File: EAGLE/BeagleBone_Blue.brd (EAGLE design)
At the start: 86.4 x 54.6 mm, 302 parts, among them J2 SERVO_HEADERS_8X, M1 JST_ZH_2, M2 JST_ZH_2, M3 JST_ZH_2, M4 JST_ZH_2, Q1 MOSFET-N, U1 TCAN1051HV, U10 TXS0108ERGYR, U13 EMMC, U2 SN74LV1T126DBVR, U3 TPD4S012DRY, U4 TPD4S012DRY, U5 24LC_32AT-I/OT, U6 SN74LVC1G07_DCK_5, U7 WL1835MODGBMOCT, U8 TPS2105_DBV_5, U9 TXS0108ERGYR, X2 SCHA5B0200, X3 USB1, X4 10118192-0001LF, Y1 24 MHz, Y2 32.768kHz

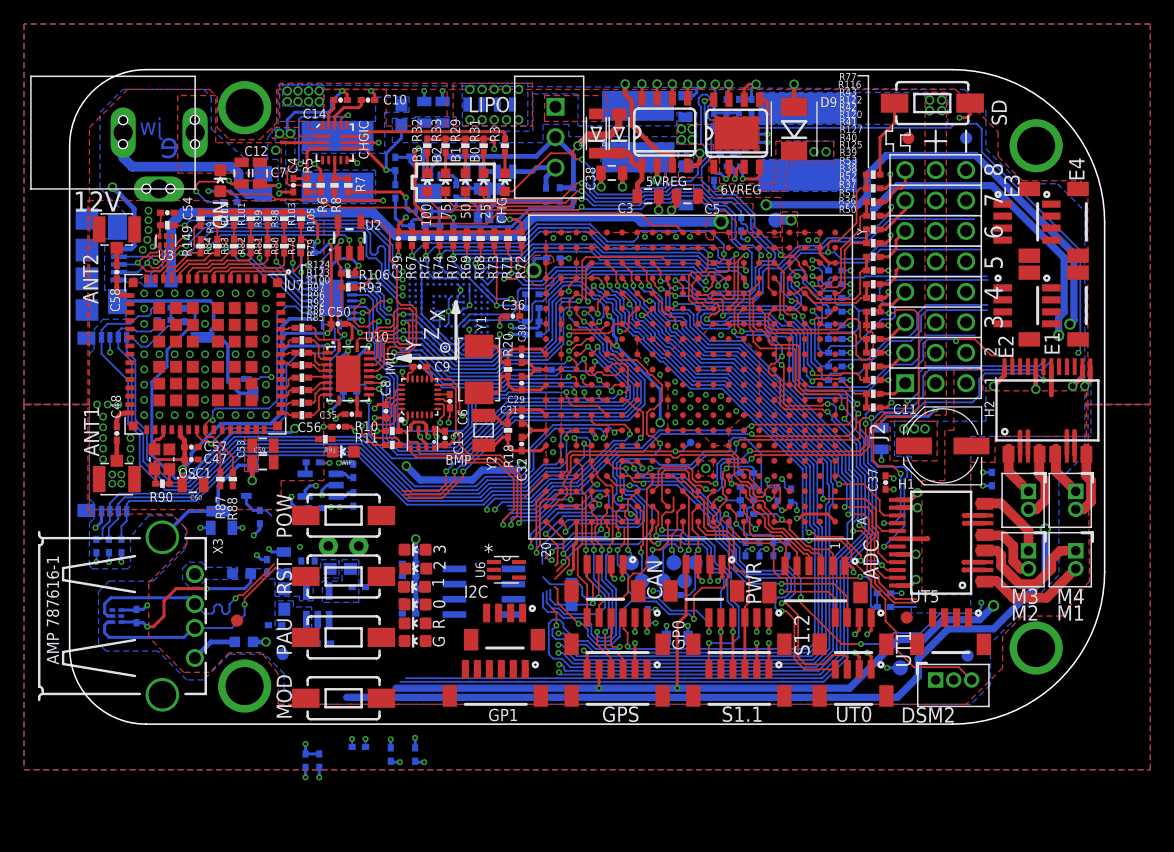
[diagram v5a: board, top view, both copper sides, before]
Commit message: Cleaned up top side silkscreen
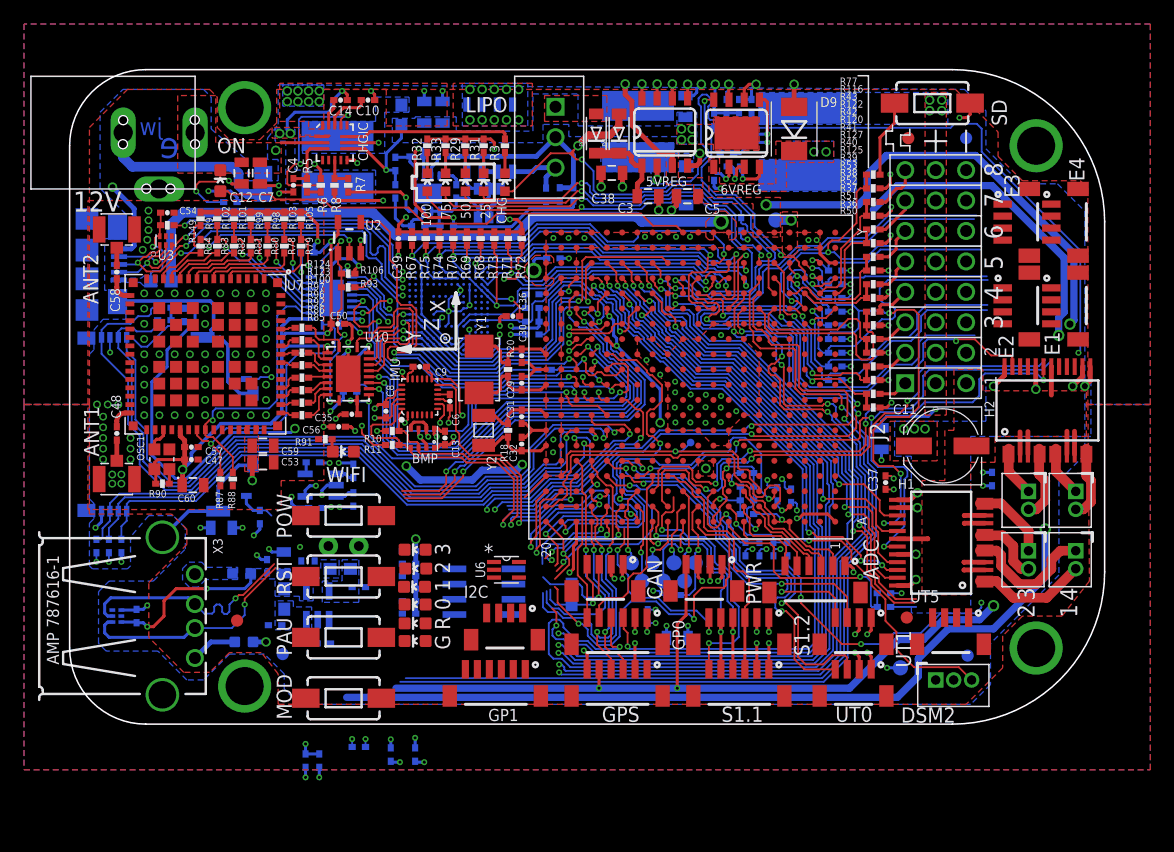
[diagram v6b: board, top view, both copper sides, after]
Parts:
- moved U$5 0.76 mm to (32.2, -23.3)
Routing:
- net N$20: track 0.00 -> 1.10 mm
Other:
- board text added: "1"
- board text added: "2"
- board text added: "3"
- board text added: "4"

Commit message: Updates to silkscreen.
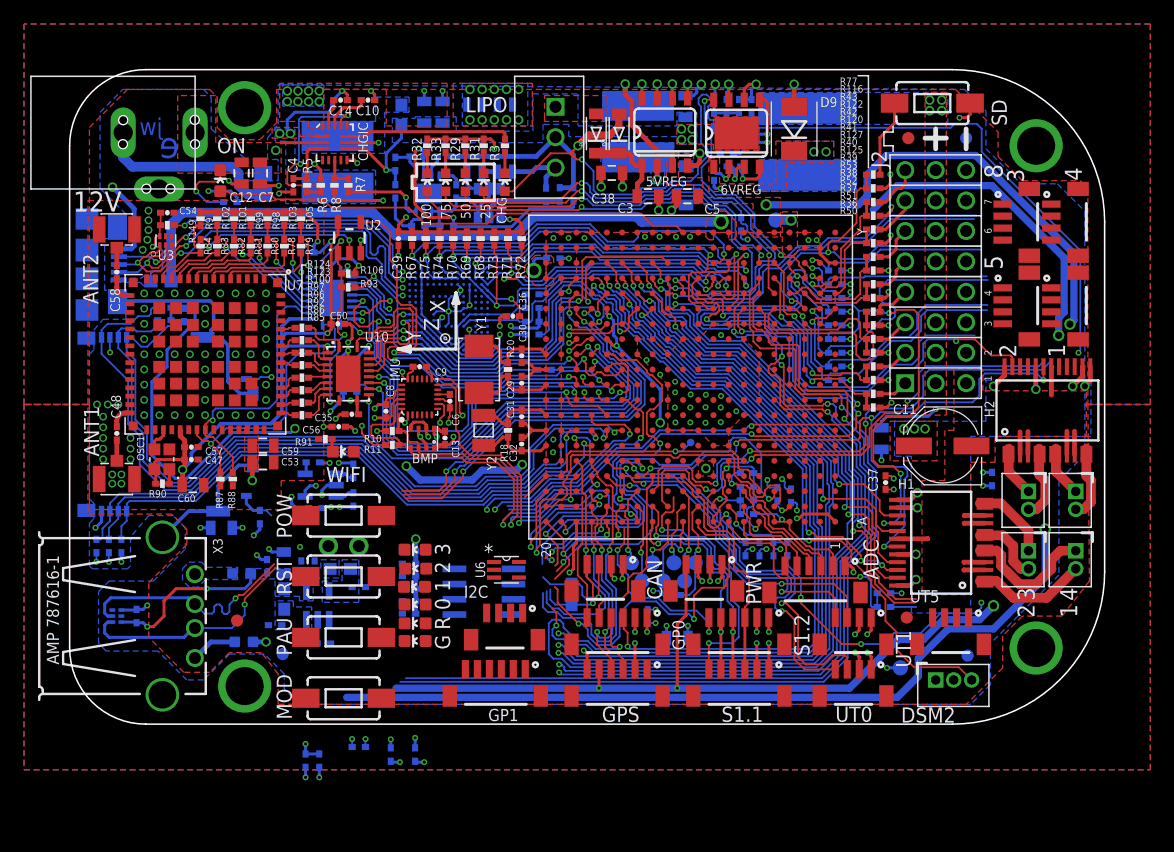
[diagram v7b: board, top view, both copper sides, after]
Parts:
- GND, WP: value TESTPAD/W_HOLE_1X1 -> GHI2_TESTPAD/W_HOLE_1X1; device GHI2:TESTPAD/W_HOLE_1X1 -> BeagleBone_Blue:GHI2_TESTPAD/W_HOLE_1X1
- J2: value SERVO_HEADERS_8X -> STRAWSON_EAGLE_LIB_SERVO_HEADERS_8X; device Strawson_Eagle_Lib:3X8_0.1"_HEADER -> BeagleBone_Blue:STRAWSON_EAGLE_LIB_3X8_0.1"_HEADER
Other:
- board text added: "5"
- board text added: "6"
- board text added: "7"
- board text added: "8"
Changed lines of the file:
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@@
 <wire x1="65.786" y1="-0.508" x2="66.6496" y2="-0.508" width="0.127" layer="21"/>
 <wire x1="66.6496" y1="-0.508" x2="66.6496" y2="-8.1788" width="0.127" layer="21"/>
-<wire x1="68.7324" y1="-6.8326" x2="68.7324" y2="-6.1976" width="0.127" layer="21"/>
-<wire x1="68.7324" y1="-6.1976" x2="68.1228" y2="-6.1976" width="0.127" layer="21"/>
-<wire x1="68.1228" y1="-6.1976" x2="68.1228" y2="-6.2738" width="0.127" layer="21"/>
-<wire x1="68.1228" y1="-6.1976" x2="68.1228" y2="-5.1308" width="0.127" layer="21"/>
-<wire x1="68.1228" y1="-5.1308" x2="68.6562" y2="-5.1308" width="0.127" layer="21"/>
-<wire x1="68.6562" y1="-5.1308" x2="68.6562" y2="-4.6228" width="0.127" layer="21"/>
-<text x="68.0466" y="-30.9372" size="1.27" layer="21" rot="R90">J2</text>
+<wire x1="68.707" y1="-6.858" x2="68.707" y2="-6.35" width="0.127" layer="21"/>
+<wire x1="68.707" y1="-6.35" x2="67.945" y2="-6.35" width="0.127" layer="21"/>
+<wire x1="67.945" y1="-6.35" x2="67.945" y2="-5.207" width="0.127" layer="21"/>
+<wire x1="67.945" y1="-5.207" x2="68.707" y2="-5.207" width="0.127" layer="21"/>
+<wire x1="68.707" y1="-5.207" x2="68.707" y2="-4.699" width="0.127" layer="21"/>
+<text x="68.1736" y="-8.2042" size="1.27" layer="21" rot="R90">J2</text>
 <wire x1="49.5808" y1="-36.322" x2="49.5808" y2="-41.8846" width="0.127" layer="22"/>
 <wire x1="51.308" y1="-41.783" x2="51.308" y2="-36.1442" width="0.127" layer="22"/>
@@
 <text x="84.074" y="-44.323" size="1.4224" layer="21" rot="R90">4</text>
 <circle x="6.985" y="-15.367" radius="0.0254" width="0.4064" layer="21"/>
+<wire x1="72.263" y1="-4.953" x2="72.263" y2="-6.604" width="0.4064" layer="21"/>
+<wire x1="71.374" y1="-5.715" x2="73.152" y2="-5.715" width="0.4064" layer="21"/>
+<wire x1="74.803" y1="-6.604" x2="74.803" y2="-4.953" width="0.4064" layer="21"/>
+<text x="76.327" y="-7.874" size="1.524" layer="21" ratio="12" rot="R270">8</text>
+<text x="83.058" y="-24.003" size="1.4224" layer="21" rot="R90">1</text>
+<text x="84.455" y="-9.271" size="1.4224" layer="21" rot="R90">4</text>
+<text x="78.994" y="-24.003" size="1.4224" layer="21" rot="R90">2</text>
+<text x="79.629" y="-9.398" size="1.4224" layer="21" rot="R90">3</text>
+<text x="76.327" y="-15.494" size="1.524" layer="21" ratio="12" rot="R270">5</text>
+<text x="76.327" y="-10.795" size="0.6096" layer="21" ratio="12" rot="R270">7</text>
+<text x="76.327" y="-13.208" size="0.6096" layer="21" ratio="12" rot="R270">6</text>
+<text x="76.327" y="-18.415" size="0.6096" layer="21" ratio="12" rot="R270">4</text>
+<text x="76.327" y="-20.955" size="0.6096" layer="21" ratio="12" rot="R270">3</text>
+<text x="76.327" y="-23.368" size="0.6096" layer="21" ratio="12" rot="R270">2</text>
+<text x="76.327" y="-25.527" size="0.6096" layer="21" ratio="12" rot="R270">1</text>
 </plain>
 <attributes>
@@
 <attribute name="VALUE" x="63.881" y="-6.858" size="1.27" layer="27" rot="R90"/>
 </element>
-<element name="E1" library="Strawson_Eagle_Lib" package="JST_SH_4_SMD" value="JST_SH_4" x="83.185" y="-18.669" smashed="yes" rot="R90">
-<attribute name="NAME" x="81.3435" y="-21.8567" size="1.27" layer="25" rot="R270"/>
-</element>
-<element name="E2" library="Strawson_Eagle_Lib" package="JST_SH_4_SMD" value="JST_SH_4" x="79.121" y="-18.669" smashed="yes" rot="R90">
-<attribute name="NAME" x="77.4954" y="-22.1234" size="1.27" layer="25" rot="R270"/>
-</element>
-<element name="E3" library="Strawson_Eagle_Lib" package="JST_SH_4_SMD" value="JST_SH_4" x="79.121" y="-11.684" smashed="yes" rot="R90">
-<attribute name="NAME" x="77.9907" y="-8.6995" size="1.27" layer="25" rot="R270"/>
-</element>
-<element name="E4" library="Strawson_Eagle_Lib" package="JST_SH_4_SMD" value="JST_SH_4" x="83.185" y="-11.684" smashed="yes" rot="R90">
-<attribute name="NAME" x="83.4009" y="-7.3152" size="1.27" layer="25" rot="R270"/>
-</element>
+<element name="E1" library="Strawson_Eagle_Lib" package="JST_SH_4_SMD" value="JST_SH_4" x="83.185" y="-18.669" smashed="yes" rot="R90"/>
+<element name="E2" library="Strawson_Eagle_Lib" package="JST_SH_4_SMD" value="JST_SH_4" x="79.121" y="-18.669" smashed="yes" rot="R90"/>
+<element name="E3" library="Strawson_Eagle_Lib" package="JST_SH_4_SMD" value="JST_SH_4" x="79.121" y="-11.684" smashed="yes" rot="R90"/>
+<element name="E4" library="Strawson_Eagle_Lib" package="JST_SH_4_SMD" value="JST_SH_4" x="83.185" y="-11.684" smashed="yes" rot="R90"/>
 <element name="GPS" library="Strawson_Eagle_Lib" package="JST_SH_6" value="JST_SH_6" x="43.18" y="-50.038" smashed="yes">
 <attribute name="NAME" x="47.5615" y="-53.1495" size="1.27" layer="25" rot="R180"/>
@@
 <attribute name="VALUE" x="52.832" y="-41.91" size="0.8128" layer="28" rot="MR0"/>
 </element>
-<element name="J2" library="Strawson_Eagle_Lib" package="3X8_0.1&quot;_HEADER" value="SERVO_HEADERS_8X" x="72.263" y="-8.382" smashed="yes"/>
+<element name="J2" library="BeagleBone_Blue" package="STRAWSON_EAGLE_LIB_3X8_0.1&quot;_HEADER" value="STRAWSON_EAGLE_LIB_SERVO_HEADERS_8X" x="72.263" y="-8.382" smashed="yes"/>
 <element name="U5" library="Microchip-24LCxxx" package="SOT95P290X145-5N" value="24LC_32AT-I/OT" x="20.9423" y="-34.671" smashed="yes" rot="MR0">
 <attribute name="MPN" value="24LC32AT-I/OT" x="20.9423" y="-34.671" size="1.778" layer="28" rot="MR0" display="off"/>
@@
 <attribute name="VALUE" x="7.46" y="-41.0929" size="0.8128" layer="27" ratio="12" rot="R270"/>
 </element>
-<element name="WP" library="GHI2" package="TESTPAD/W_HOLE_1X1" value="TESTPAD/W_HOLE_1X1" x="21.59" y="-39.751" smashed="yes" rot="MR0">
+<element name="WP" library="BeagleBone_Blue" package="GHI2_TESTPAD/W_HOLE_1X1" value="GHI2_TESTPAD/W_HOLE_1X1" x="21.59" y="-39.751" smashed="yes" rot="MR0">
 <attribute name="VALUE" x="22.86" y="-42.291" size="0.8128" layer="28" ratio="12" rot="MR0"/>
 <attribute name="NAME" x="20.6248" y="-38.9382" size="0.8128" layer="26" ratio="12" rot="MR270"/>
@@
 <attribute name="NAME" x="70.104" y="-44.45" size="1.016" layer="25"/>
 </element>
-<element name="GND" library="GHI2" package="TESTPAD/W_HOLE_1X1" value="TESTPAD/W_HOLE_1X1" x="24.13" y="-39.751" rot="MR0"/>
+<element name="GND" library="BeagleBone_Blue" package="GHI2_TESTPAD/W_HOLE_1X1" value="GHI2_TESTPAD/W_HOLE_1X1" x="24.13" y="-39.751" rot="MR0"/>
 <element name="C59" library="SparkFun-Capacitors" package="0805" value="10uF" x="16.129" y="-32.766" smashed="yes">
 <attribute name="NAME" x="17.653" y="-32.131" size="0.6096" layer="25"/>

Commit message: Updated layout.
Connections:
- net LED_GRN: now also GP1.6; no longer GP1.5
- net LED_RED: now also GP1.5; no longer GP1.6
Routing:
- net USB1_VBUS: track 123.9 -> 14.0 mm, vias 4 -> 2
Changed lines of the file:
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@@
 <layers>
 <layer number="1" name="Top" color="4" fill="1" visible="yes" active="yes"/>
-<layer number="2" name="Route2" color="1" fill="3" visible="no" active="yes"/>
+<layer number="2" name="Route2" color="1" fill="3" visible="yes" active="yes"/>
 <layer number="3" name="Route3" color="4" fill="3" visible="no" active="no"/>
 <layer number="4" name="Route4" color="1" fill="4" visible="no" active="no"/>
@@
 <wire x1="66.675" y1="-33.7312" x2="66.675" y2="-38.6588" width="0.1524" layer="16"/>
 <wire x1="41.021" y1="-50.4698" x2="40.8432" y2="-50.292" width="0.1524" layer="16"/>
-<contactref element="GP1" pad="5"/>
-<wire x1="34.02" y1="-50.038" x2="29.706" y2="-47.6758" width="0" layer="19" extent="1-1"/>
-<wire x1="40.8432" y1="-50.292" x2="34.02" y2="-50.038" width="0" layer="19" extent="1-1"/>
+<contactref element="GP1" pad="6"/>
+<wire x1="33.02" y1="-50.038" x2="29.706" y2="-47.6758" width="0" layer="19" extent="1-1"/>
+<wire x1="40.8432" y1="-50.292" x2="33.02" y2="-50.038" width="0" layer="19" extent="1-1"/>
 </signal>
 <signal name="MODE_BTN">
@@
 <wire x1="41.275" y1="-49.8602" x2="41.0464" y2="-49.6316" width="0.1524" layer="16"/>
 <wire x1="41.0464" y1="-49.6316" x2="40.8432" y2="-49.6316" width="0.1524" layer="16"/>
-<contactref element="GP1" pad="6"/>
-<wire x1="33.02" y1="-50.038" x2="29.706" y2="-46.2026" width="0" layer="19" extent="1-1"/>
-<wire x1="40.8432" y1="-49.6316" x2="33.02" y2="-50.038" width="0" layer="19" extent="1-1"/>
+<contactref element="GP1" pad="5"/>
+<wire x1="34.02" y1="-50.038" x2="29.706" y2="-46.2026" width="0" layer="19" extent="1-1"/>
+<wire x1="40.8432" y1="-49.6316" x2="34.02" y2="-50.038" width="0" layer="19" extent="1-1"/>
 </signal>
 <signal name="PAUSE_BTN">
@@
 <vertex x="17.145" y="-44.323"/>
 <vertex x="17.145" y="-46.736"/>
-<vertex x="20.193" y="-46.736"/>
-<vertex x="20.193" y="-44.831"/>
+<vertex x="20.066" y="-46.736"/>
+<vertex x="20.066" y="-44.831"/>
 <vertex x="18.669" y="-44.831"/>
 <vertex x="18.669" y="-44.323"/>
@@
 <vertex x="14.7066" y="-42.4942"/>
 </polygon>
-<via x="82.5246" y="-22.1742" extent="1-16" drill="0.6"/>
-<wire x1="82.5246" y1="-22.1742" x2="82.5246" y2="-37.211" width="0.6096" layer="2"/>
-<via x="81.407" y="-38.3286" extent="1-16" drill="0.6"/>
-<wire x1="81.407" y1="-38.3286" x2="81.407" y2="-42.3418" width="0.6096" layer="16"/>
-<wire x1="81.407" y1="-42.3418" x2="77.089" y2="-46.6598" width="0.6096" layer="16"/>
-<wire x1="77.089" y1="-46.6598" x2="73.3044" y2="-46.6598" width="0.6096" layer="16"/>
-<wire x1="73.3044" y1="-46.6598" x2="70.8152" y2="-49.149" width="0.6096" layer="16"/>
-<wire x1="70.8152" y1="-49.149" x2="70.8152" y2="-50.6222" width="0.6096" layer="16"/>
-<wire x1="70.8152" y1="-50.6222" x2="69.0626" y2="-52.3748" width="0.6096" layer="16"/>
-<wire x1="69.0626" y1="-52.3748" x2="23.114" y2="-52.3748" width="0.6096" layer="16"/>
-<wire x1="82.9818" y1="-15.6972" x2="82.9818" y2="-20.2438" width="0.6096" layer="16"/>
-<wire x1="82.9818" y1="-20.2438" x2="82.5246" y2="-20.701" width="0.6096" layer="16"/>
-<wire x1="82.5246" y1="-20.701" x2="82.5246" y2="-22.1742" width="0.6096" layer="16"/>
-<wire x1="81.407" y1="-38.3286" x2="82.5246" y2="-37.211" width="0.6096" layer="2"/>
-<wire x1="76.962" y1="-9.6774" x2="82.9818" y2="-15.6972" width="0.6096" layer="16"/>
 <wire x1="7.874" y1="-45.593" x2="6.985" y2="-46.482" width="0.254" layer="1"/>
 <wire x1="6.985" y1="-46.482" x2="6.477" y2="-46.482" width="0.254" layer="1"/>
 <contactref element="C61" pad="2"/>
-<wire x1="76.962" y1="-9.6774" x2="69.0626" y2="-9.6774" width="0.6096" layer="16"/>
-<wire x1="69.0626" y1="-9.6774" x2="67.056" y2="-11.684" width="0.6096" layer="16"/>
 <contactref element="U8" pad="4"/>
-<wire x1="19.751" y1="-43.5102" x2="23.114" y2="-52.3748" width="0" layer="19" extent="16-16"/>
+<wire x1="16.4338" y1="-42.037" x2="15.113" y2="-42.037" width="0" layer="19" extent="16-16"/>
+<wire x1="17.8689" y1="-42.048" x2="16.4719" y2="-41.9989" width="0" layer="19" extent="16-16"/>
+<wire x1="17.907" y1="-43.3206" x2="17.8689" y2="-42.048" width="0" layer="19" extent="16-16"/>
+<wire x1="19.3294" y1="-42.1132" x2="17.8689" y2="-42.048" width="0" layer="19" extent="16-16"/>
+<wire x1="20.447" y1="-42.1132" x2="19.3294" y2="-42.1132" width="0" layer="19" extent="16-16"/>
+<wire x1="21.7306" y1="-41.656" x2="20.447" y2="-42.1132" width="0" layer="19" extent="16-16"/>
+<wire x1="19.751" y1="-43.5102" x2="19.3294" y2="-42.1132" width="0" layer="19" extent="16-16"/>
 </signal>
 <signal name="USB0_VBUS">
